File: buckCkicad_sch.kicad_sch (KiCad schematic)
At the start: 33 parts, among them Q1 SSM3K15AMFV,L3F, U6 SiC437BED-T1-GE3

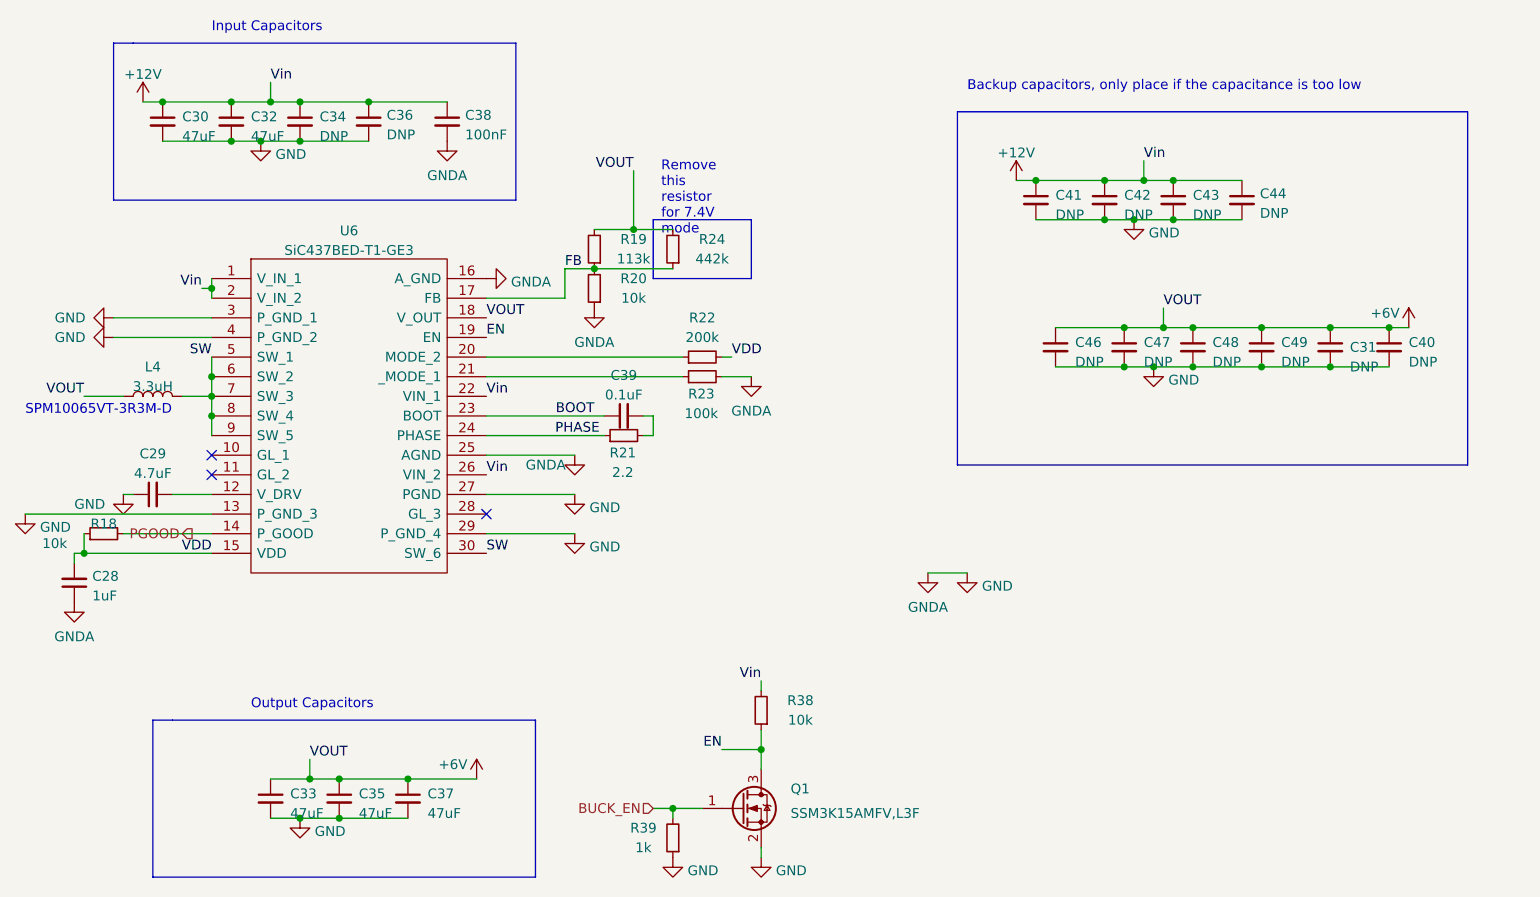
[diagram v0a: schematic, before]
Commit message: Engine Controller: Added in ads and pressure sensor
Circuit for both 5v and 10v
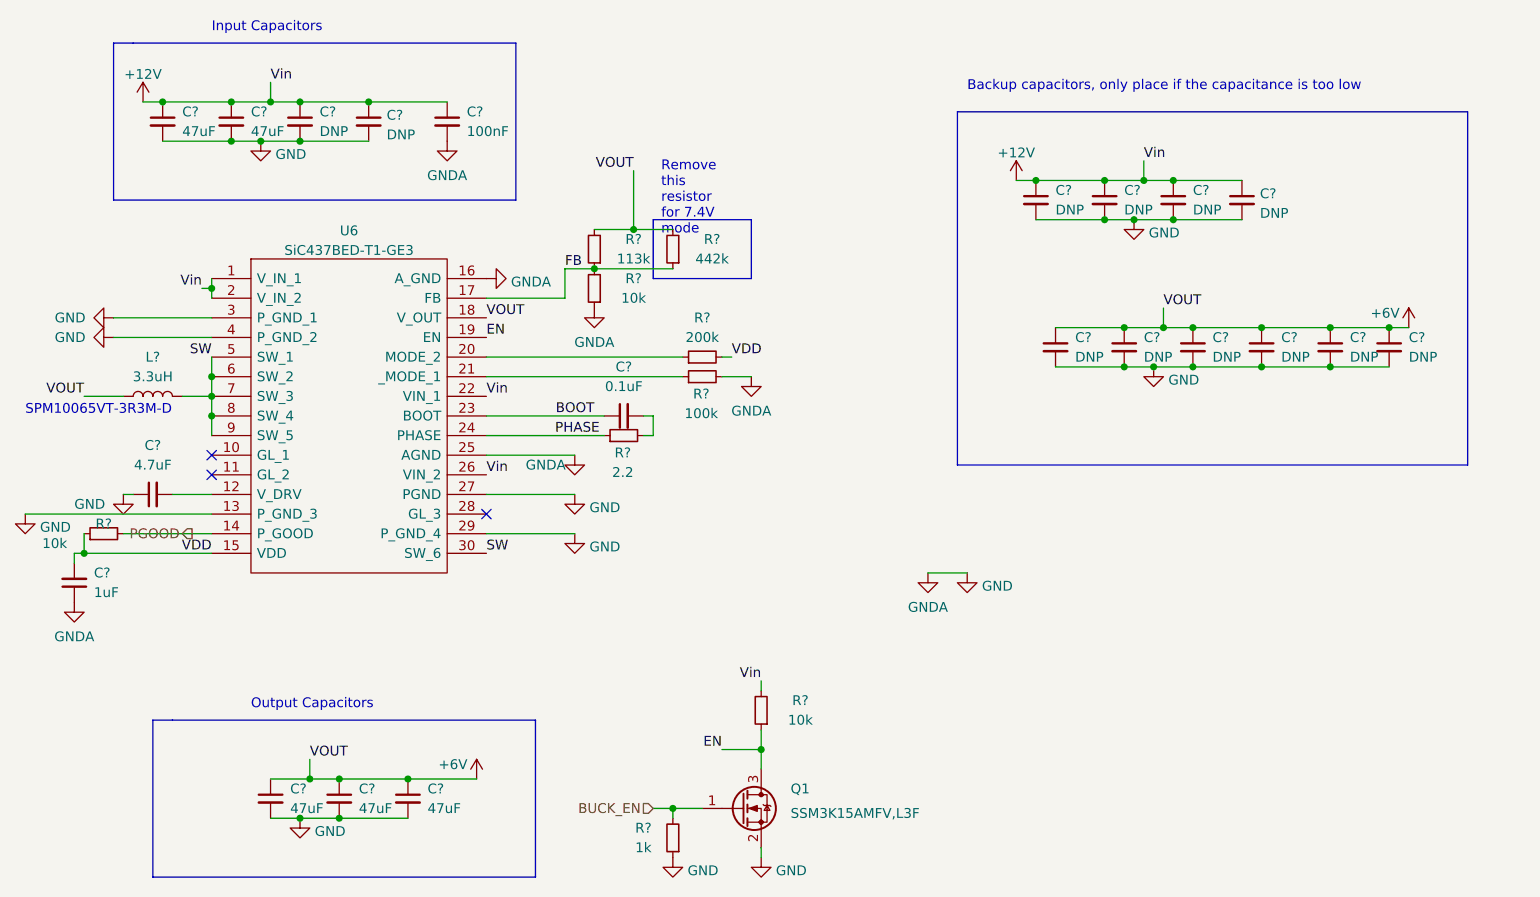
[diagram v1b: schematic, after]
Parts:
- renumbered C49 to C?, C36 to C?, C33 to C?, C37 to C?, C32 to C?, C29 to C?, C40 to C?, C42 to C?, C30 to C?, C48 to C?, C35 to C?, C46 to C?, C31 to C?, C43 to C?, C41 to C?, C47 to C?, C34 to C?, C44 to C?, C38 to C?, C28 to C?, C39 to C?, L4 to L?, R19 to R?, R38 to R?, R24 to R?, R23 to R?, R39 to R?, R20 to R?, R18 to R?, R21 to R?, R22 to R?

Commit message: Completed schematics
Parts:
- gave numbers to parts that had none: 31

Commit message: Finished schematic
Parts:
- R20: value 113k -> 130k
- R23: value 442k -> 294k
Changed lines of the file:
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@@
       (effects (font (size 1.27 1.27)))
     )
-    (property "Value" "113k" (at 129.54 48.2569 0)
+    (property "Value" "130k" (at 129.54 48.2569 0)
       (effects (font (size 1.27 1.27)))
     )
@@
       (effects (font (size 1.27 1.27)))
     )
-    (property "Value" "442k" (at 139.7 48.2569 0)
-      (effects (font (size 1.27 1.27)))
-    )
+    (property "Value" "294k" (at 139.7 48.2569 0)
+      (effects (font (size 1.27 1.27)))
+    )

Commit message: update
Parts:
- L4: footprint iclr:IND_SPM10065VT-3R3M-D -> Inductor_SMD:L_0402_1005Metric
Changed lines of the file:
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@@
       (effects (font (size 1.27 1.27)))
     )
-    (property "Footprint" "iclr:IND_SPM10065VT-3R3M-D" (at 67.31 66.04 0)
+    (property "Footprint" "Inductor_SMD:L_0402_1005Metric" (at 67.31 66.04 0)
       (effects (font (size 1.27 1.27)) hide)
     )

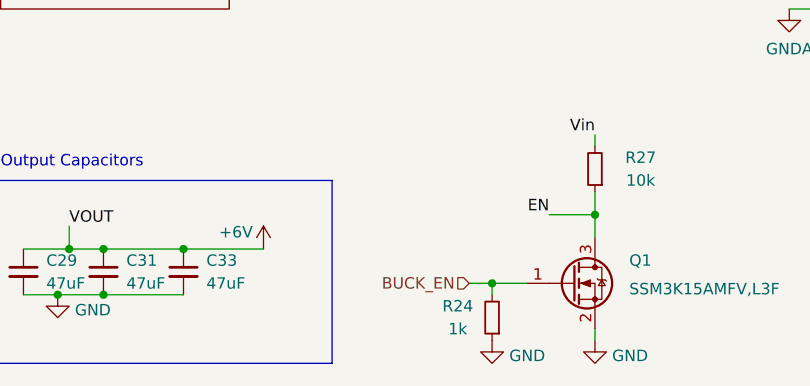
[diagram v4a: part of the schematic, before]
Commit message: Schematic done, components layed out, sensors wired up
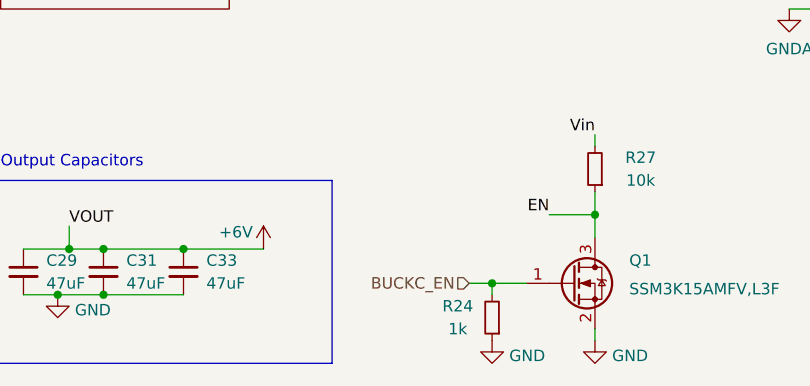
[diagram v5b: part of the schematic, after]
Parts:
- L4: footprint Inductor_SMD:L_0402_1005Metric -> iclr:IND_SRP6540-390M
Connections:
- net BUCK_EN renamed BUCKC_EN
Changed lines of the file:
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@@
     (effects (font (size 1.27 1.27)) (justify right bottom))
   )
-  (hierarchical_label "BUCK_EN" (shape input) (at 132.08 119.38 180) (fields_autoplaced)
+  (hierarchical_label "BUCKC_EN" (shape input) (at 132.08 119.38 180) (fields_autoplaced)
     (effects (font (size 1.27 1.27)) (justify right))
   )
@@
       (effects (font (size 1.27 1.27)))
     )
-    (property "Footprint" "Inductor_SMD:L_0402_1005Metric" (at 67.31 66.04 0)
-      (effects (font (size 1.27 1.27)) hide)
-    )
-    (property "Datasheet" "~" (at 67.31 66.04 0)
-      (effects (font (size 1.27 1.27)) hide)
-    )
+    (property "Footprint" "iclr:IND_SRP6540-390M" (at 67.31 66.04 0)
+      (effects (font (size 1.27 1.27)) hide)
+    )
+    (property "Datasheet" "  (layer \"F.Cu\")" (at 67.31 66.04 0)
+      (effects (font (size 1.27 1.27)) hide)
+    )

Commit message: v1.2
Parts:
- removed C36, C38, C39, C40, C42, C43, C44, C45: DNP, Capacitor_SMD:C_1206_3216Metric, symbol Device:C_Small
- removed C37, C41: DNP, Capacitor_SMD:C_0805_2012Metric, symbol Device:C_Small
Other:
- note removed: "Backup capacitors, only place if the capacitance is too low"

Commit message: More Based
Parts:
- renumbered R19 to R25, R20 to R26, R21 to R27, R22 to R28, R23 to R29, R24 to R30, R25 to R31, R26 to R32, R27 to R33

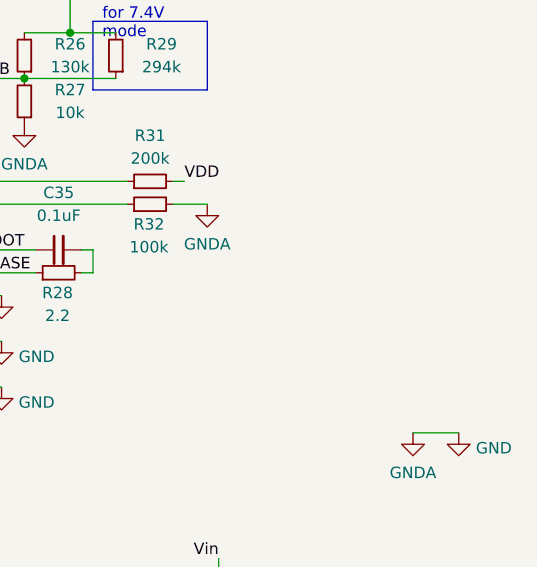
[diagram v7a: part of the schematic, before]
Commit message: Lol pyro buck out  was shorting straight to ground
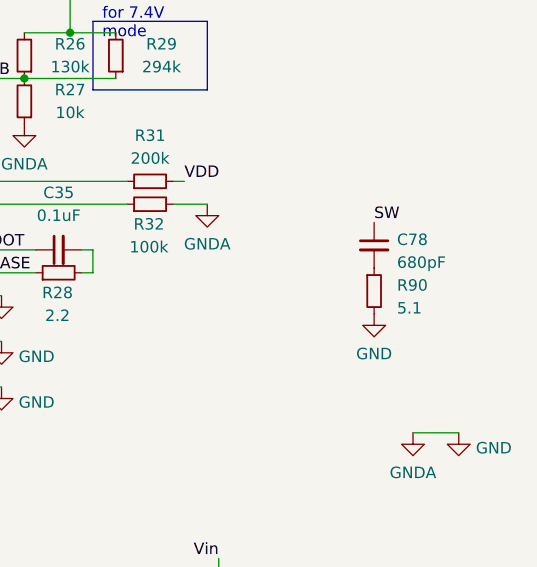
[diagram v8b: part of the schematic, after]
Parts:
- added C78: 680pF, Capacitor_SMD:C_0603_1608Metric, symbol Device:C_Small
- added R90: 5.1, Resistor_SMD:R_0603_1608Metric, symbol Device:R_Small
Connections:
- net GND: now also R90.2
- net SW: now also C78.1
- new net: C78.2, R90.1
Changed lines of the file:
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@@
+    (effects (font (size 1.27 1.27)) (justify left bottom))
+  )
+  (label "SW" (at 163.322 65.532 0) (fields_autoplaced)
     (effects (font (size 1.27 1.27)) (justify left bottom))
   )
@@
     )
   )
+  (symbol (lib_id "Device:R_Small") (at 163.322 73.152 0) (unit 1)
+    (in_bom yes) (on_board yes) (dnp no) (fields_autoplaced)
+    (property "Reference" "R90" (at 165.862 72.517 0)
+      (effects (font (size 1.27 1.27)) (justify left))
+    )
+    (property "Value" "5.1" (at 165.862 75.057 0)
+      (effects (font (size 1.27 1.27)) (justify left))
+    )
+    (property "Footprint" "Resistor_SMD:R_0603_1608Metric" (at 163.322 73.152 0)
+      (effects (font (size 1.27 1.27)) hide)
+    )
+    (property "Datasheet" "~" (at 163.322 73.152 0)
+      (effects (font (size 1.27 1.27)) hide)
+    )
+    (pin "1")
+    (pin "2")
+    (instances
+      (project "Ricardo-Stark"
+        (path "/7db990e4-92e1-4f99-b4d2-435bbec1ba83/6c17bf58-bab3-4fa6-ad33-cca9e388d73c"
+          (reference "R90") (unit 1)
+        )
+      )
+      (project "PDU"
+        (path "/e63e39d7-6ac0-4ffd-8aa3-1841a4541b55/e469982c-3823-4665-9e6d-e90b00c2da09"
+          (reference "R37") (unit 1)
+        )
+      )
+    )
+  )
+  (symbol (lib_id "power:GND") (at 163.322 75.692 0) (unit 1)
+    (in_bom yes) (on_board yes) (dnp no) (fields_autoplaced)
+    (property "Reference" "#PWR0174" (at 163.322 82.042 0)
+      (effects (font (size 1.27 1.27)) hide)
+    )
+    (property "Value" "GND" (at 163.322 80.1354 0)
+      (effects (font (size 1.27 1.27)))
+    )
+    (property "Footprint" "" (at 163.322 75.692 0)
+      (effects (font (size 1.27 1.27)) hide)
+    )
+    (property "Datasheet" "" (at 163.322 75.692 0)
+      (effects (font (size 1.27 1.27)) hide)
+    )
+    (pin "1")
+    (instances
+      (project "Ricardo-Stark"
+        (path "/7db990e4-92e1-4f99-b4d2-435bbec1ba83/6c17bf58-bab3-4fa6-ad33-cca9e388d73c"
+          (reference "#PWR0174") (unit 1)
+        )
+      )
+      (project "PDU"
+        (path "/e63e39d7-6ac0-4ffd-8aa3-1841a4541b55/e469982c-3823-4665-9e6d-e90b00c2da09"
+          (reference "#PWR017") (unit 1)
+        )
+      )
+    )
+  )
   (symbol (lib_id "Device:C_Small") (at 77.47 30.48 0) (unit 1)
     (in_bom yes) (on_board yes) (dnp no) (fields_autoplaced)
@@
         )
       )
+    )
+  )
+  (symbol (lib_id "Device:C_Small") (at 163.322 68.072 0) (unit 1)
+    (in_bom yes) (on_board yes) (dnp no) (fields_autoplaced)
+    (property "Reference" "C78" (at 165.862 67.4433 0)
+      (effects (font (size 1.27 1.27)) (justify left))
+    )
+    (property "Value" "680pF" (at 165.862 69.9833 0)
+      (effects (font (size 1.27 1.27)) (justify left))
+    )
+    (property "Footprint" "Capacitor_SMD:C_0603_1608Metric" (at 163.322 68.072 0)
+      (effects (font (size 1.27 1.27)) hide)
+    )
+    (property "Datasheet" "~" (at 163.322 68.072 0)
+      (effects (font (size 1.27 1.27)) hide)
+    )
+    (pin "1")
+    (pin "2")
+    (instances
+      (project "Ricardo-Stark"
+        (path "/7db990e4-92e1-4f99-b4d2-435bbec1ba83/6c17bf58-bab3-4fa6-ad33-cca9e388d73c"
+          (reference "C78") (unit 1)
+        )
+      )
+      (project "PDU"
+        (path "/e63e39d7-6ac0-4ffd-8aa3-1841a4541b55/e469982c-3823-4665-9e6d-e90b00c2da09"
+          (reference "C16") (unit 1)
+        )
+      )
